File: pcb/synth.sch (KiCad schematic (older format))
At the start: 47 parts, among them J1 Conn_01x06, SW1 SW_Push, SW10 SW_Push, SW11 SW_Push, SW12 SW_Push, SW13 SW_Push, SW14 SW_Push, SW15 SW_Push, SW16 SW_Push, SW17 SW_Push, SW18 SW_Push, SW19 SW_Push, SW2 SW_Push, SW20 SW_Push, SW21 SW_Push, SW22 SW_Push, SW23 SW_Push, SW24 SW_Push, SW3 SW_Push, SW4 SW_Push, SW5 SW_Push, SW6 SW_Push, SW7 SW_Push, SW8 SW_Push, SW9 SW_Push, U1 STM32F407VGTx, Y1 Crystal

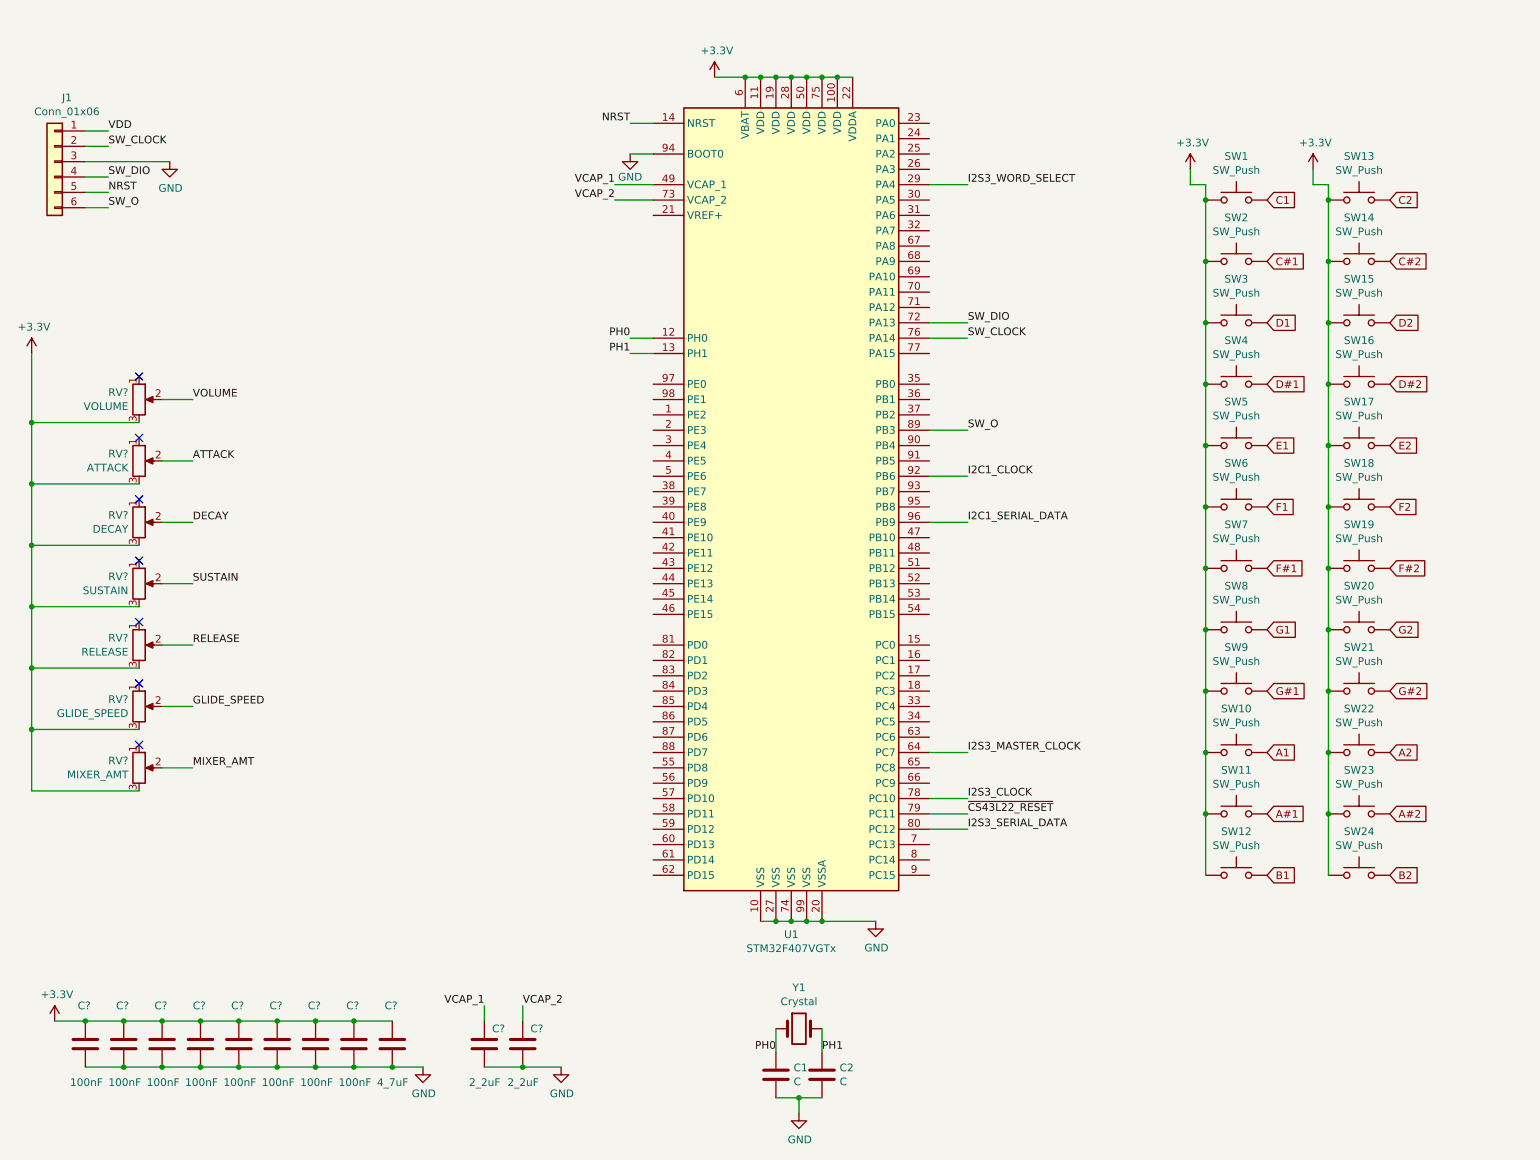
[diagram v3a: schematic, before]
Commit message: Clean up knobs and add a wave shape knob.
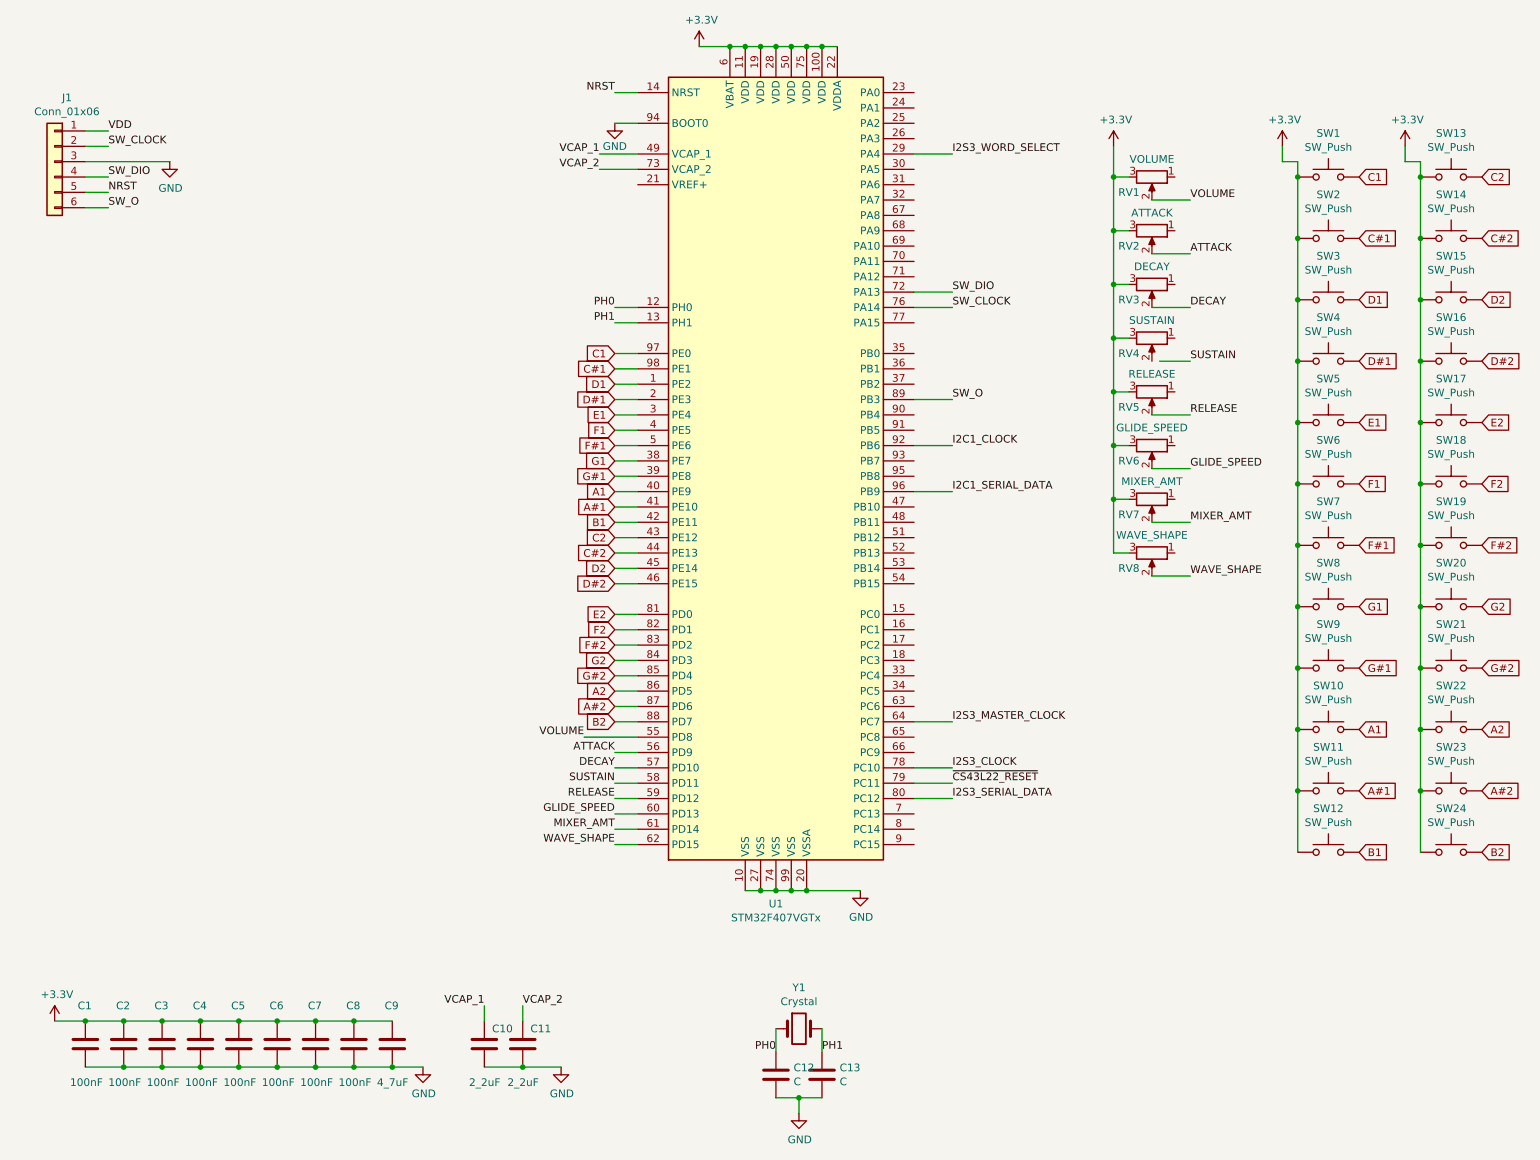
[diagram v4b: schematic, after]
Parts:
- removed RV?: VOLUME, symbol Device:R_POT
- removed RV?: ATTACK, symbol Device:R_POT
- removed RV?: DECAY, symbol Device:R_POT
- removed RV?: SUSTAIN, symbol Device:R_POT
- removed RV?: RELEASE, symbol Device:R_POT
- removed RV?: GLIDE_SPEED, symbol Device:R_POT
- removed RV?: MIXER_AMT, symbol Device:R_POT
- added RV1: VOLUME, symbol Device:R_POT
- added RV2: ATTACK, symbol Device:R_POT
- added RV3: DECAY, symbol Device:R_POT
- added RV4: SUSTAIN, symbol Device:R_POT
- added RV5: RELEASE, symbol Device:R_POT
- added RV6: GLIDE_SPEED, symbol Device:R_POT
- added RV7: MIXER_AMT, symbol Device:R_POT
- added RV8: WAVE_SHAPE, symbol Device:R_POT
- gave numbers to parts that had none: 11
- renumbered C1 to C12, C2 to C13
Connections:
- net +3V3: now also RV1.3, RV2.3, RV3.3, RV4.3, RV5.3, RV6.3, RV7.3, RV8.3
- net A#1: now also U1.41 (PE10)
- net A#2: now also U1.87 (PD6)
- net A1: now also U1.40 (PE9)
- net A2: now also U1.86 (PD5)
- net ATTACK: now also U1.56 (PD9), RV2.2
- net B1: now also U1.42 (PE11)
- net B2: now also U1.88 (PD7)
- net C#1: now also U1.98 (PE1)
- net C#2: now also U1.44 (PE13)
- net C1: now also U1.97 (PE0)
- net C2: now also U1.43 (PE12)
- net D#1: now also U1.2 (PE3)
- net D#2: now also U1.46 (PE15)
- net D1: now also U1.1 (PE2)
- net D2: now also U1.45 (PE14)
- net DECAY: now also U1.57 (PD10), RV3.2
- net E1: now also U1.3 (PE4)
- net E2: now also U1.81 (PD0)
- net F#1: now also U1.5 (PE6)
- net F#2: now also U1.83 (PD2)
- net F1: now also U1.4 (PE5)
- net F2: now also U1.82 (PD1)
- net G#1: now also U1.39 (PE8)
- net G#2: now also U1.85 (PD4)
- net G1: now also U1.38 (PE7)
- net G2: now also U1.84 (PD3)
- net GLIDE_SPEED: now also U1.60 (PD13), RV6.2
- net MIXER_AMT: now also U1.61 (PD14), RV7.2
- net RELEASE: now also U1.59 (PD12), RV5.2
- net SUSTAIN: now also U1.58 (PD11)
- net VOLUME: now also U1.55 (PD8), RV1.2
- net WAVE_SHAPE: now reaches U1.62 (PD15)
- net WAVE_SHAPE: now also RV8.2
- no-connect marks 7 -> 0
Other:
- moved on the sheet: SW1, SW10, SW11, SW12, SW13, SW14, SW15, SW16, SW17, SW18, SW19, SW2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

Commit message: Add cap values for the crystal caps, and mark unused pot legs as NC.
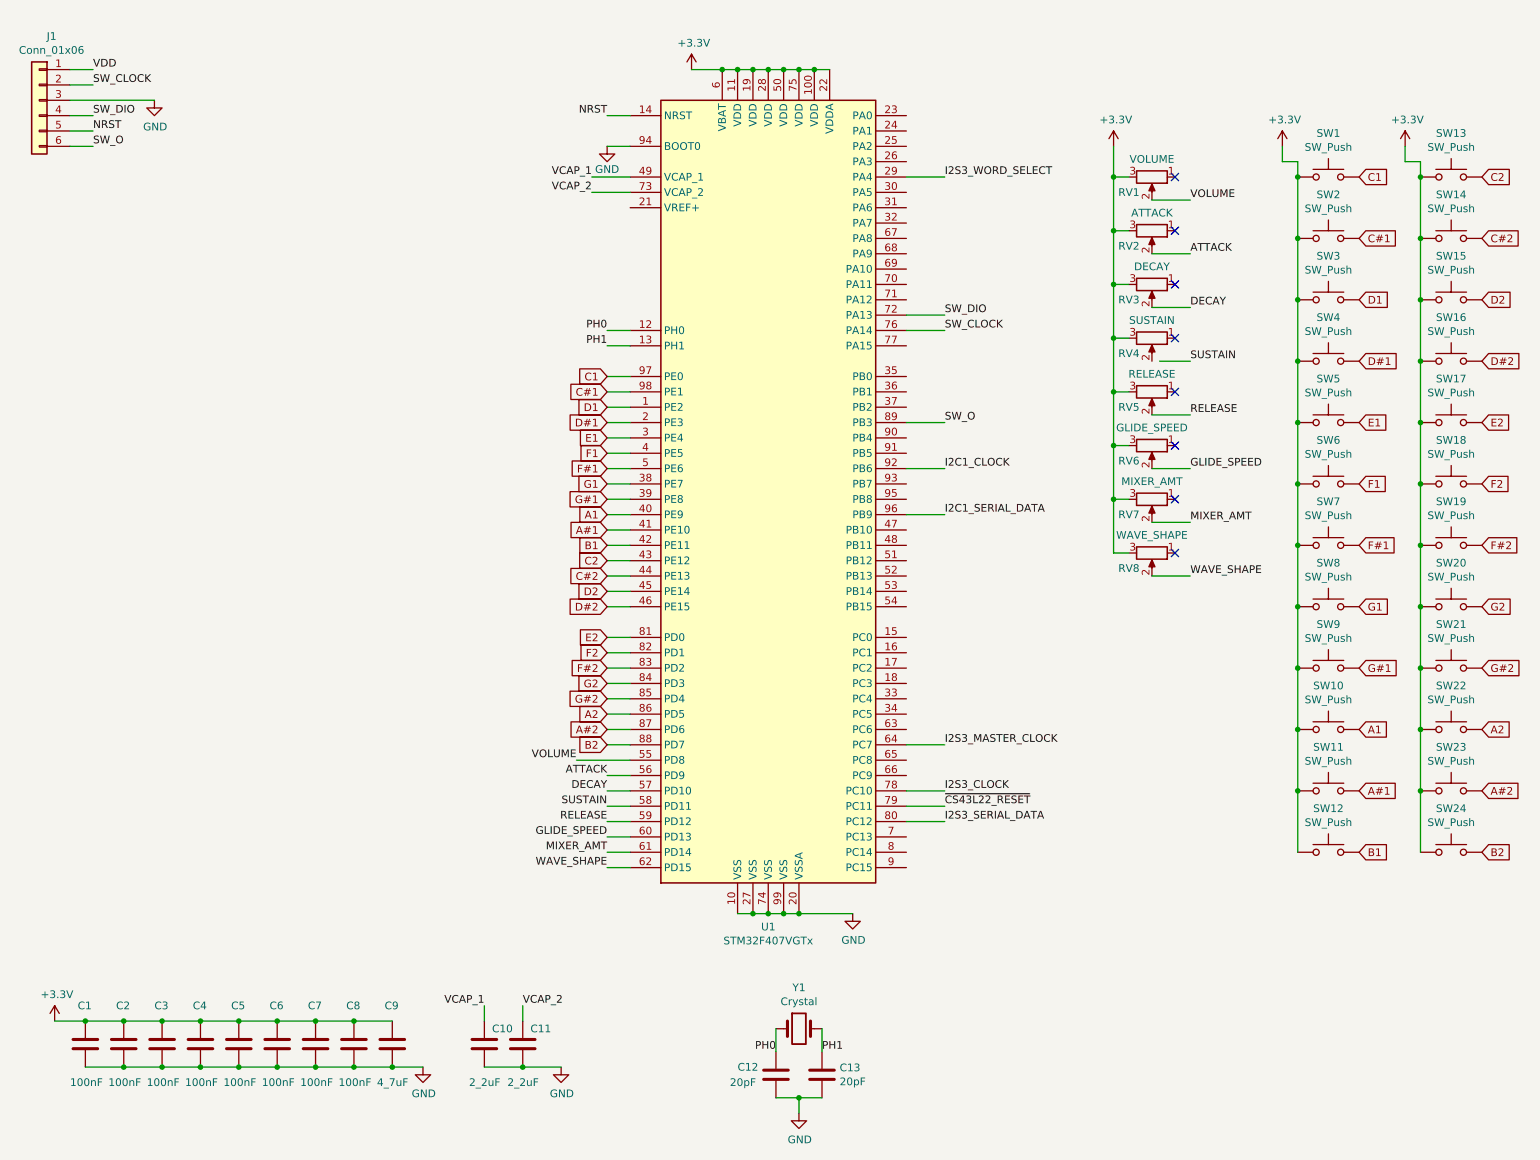
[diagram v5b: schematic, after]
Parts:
- C12, C13: value C -> 20pF
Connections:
- no-connect marks 0 -> 8
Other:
- moved on the sheet: J1, U1
